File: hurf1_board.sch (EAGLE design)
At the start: 41 parts, among them IC1 STM32F10XCXT6, J1 0R, J2 0R, X1 MINI-USB-32005-201, Y1 8MHz

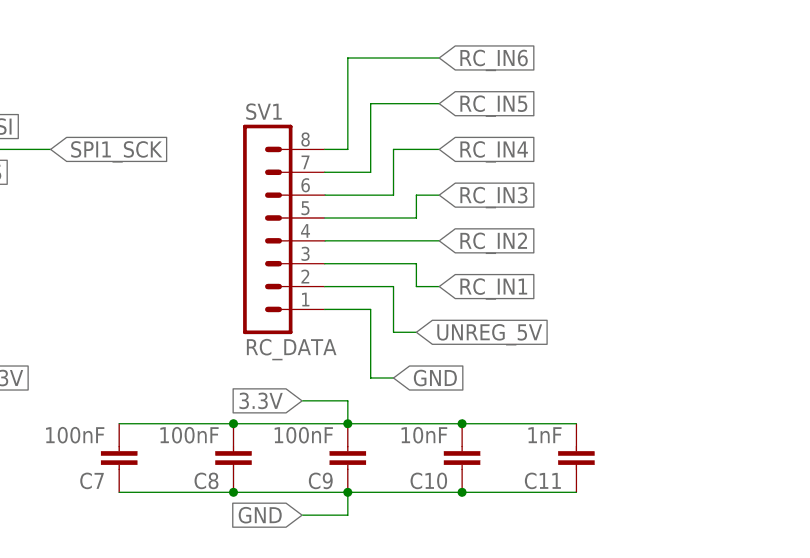
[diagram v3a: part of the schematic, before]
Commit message: Final touches to board -schematic w1 (updated)  *RC_IN port package updated from DIL -> JST-SH -board w1s1(updated)  *Schematics changes applied  *General check successful  *Signs and Logos added -Status: RTF
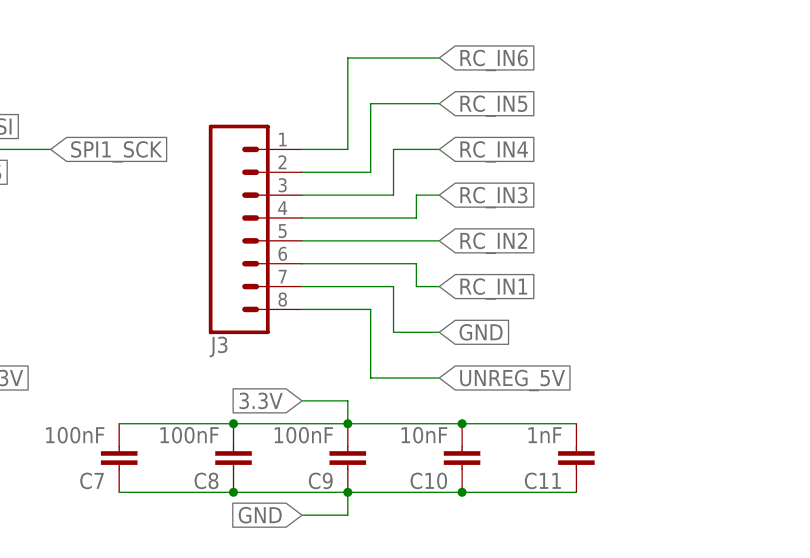
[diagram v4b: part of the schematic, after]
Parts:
- removed SV1: RC_DATA, con-lstb:MA08-1
- added J3: (no value), SparkFun-Connectors:CONN_08
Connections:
- net GND: now also J3.7; no longer SV1.1
- net RC_IN1: now also J3.6; no longer SV1.3
- net RC_IN2: now also J3.5; no longer SV1.4
- net RC_IN3: now also J3.4; no longer SV1.5
- net RC_IN4: now also J3.3; no longer SV1.6
- net RC_IN5: now also J3.2; no longer SV1.7
- net RC_IN6: now also J3.1; no longer SV1.8
- net UNREG_5V: now also J3.8; no longer SV1.2
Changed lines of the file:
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@@
 <part name="C5" library="rcl" library_urn="urn:adsk.eagle:library:334" deviceset="C-EU" device="C0603" value="100nF"/>
 <part name="C6" library="rcl" library_urn="urn:adsk.eagle:library:334" deviceset="C-EU" device="C0603" value="10nF"/>
-<part name="SV1" library="con-lstb" library_urn="urn:adsk.eagle:library:162" deviceset="MA08-1" device="" value="RC_DATA"/>
 <part name="D1" library="diode" library_urn="urn:adsk.eagle:library:210" deviceset="DIODE-2AC|CA" device="SOT23" value=" "/>
 <part name="C7" library="rcl" library_urn="urn:adsk.eagle:library:334" deviceset="C-EU" device="C0603" value="100nF"/>
@@
 <part name="ESC3" library="SparkFun-Connectors" deviceset="CONN_03" device=""/>
 <part name="ESC4" library="SparkFun-Connectors" deviceset="CONN_03" device=""/>
+<part name="J3" library="SparkFun-Connectors" deviceset="CONN_08" device=""/>
 </parts>
 <sheets>
@@
 <instance part="C5" gate="G$1" x="48.26" y="111.76"/>
 <instance part="C6" gate="G$1" x="-10.16" y="134.62"/>
-<instance part="SV1" gate="1" x="88.9" y="129.54"/>
 <instance part="D1" gate="-B1" x="53.34" y="27.94" rot="R270"/>
 <instance part="C7" gate="G$1" x="73.66" y="104.14" rot="R180"/>
@@
 <instance part="ESC3" gate="J$1" x="-53.34" y="60.96"/>
 <instance part="ESC4" gate="J$1" x="-60.96" y="48.26"/>
+<instance part="J3" gate="G$1" x="88.9" y="132.08" rot="MR180"/>
 </instances>
 <busses>
@@
 </segment>
 <segment>
-<pinref part="SV1" gate="1" pin="1"/>
-<wire x1="96.52" y1="121.92" x2="101.6" y2="121.92" width="0.1524" layer="91"/>
-<wire x1="101.6" y1="121.92" x2="101.6" y2="114.3" width="0.1524" layer="91"/>
-<wire x1="101.6" y1="114.3" x2="104.14" y2="114.3" width="0.1524" layer="91"/>
-<label x="104.14" y="114.3" size="1.778" layer="95" xref="yes"/>
+<label x="109.22" y="119.38" size="1.778" layer="95" xref="yes"/>
+<pinref part="J3" gate="G$1" pin="7"/>
+<wire x1="93.98" y1="124.46" x2="104.14" y2="124.46" width="0.1524" layer="91"/>
+<wire x1="104.14" y1="124.46" x2="104.14" y2="119.38" width="0.1524" layer="91"/>
+<wire x1="104.14" y1="119.38" x2="109.22" y2="119.38" width="0.1524" layer="91"/>
 </segment>
 <segment>
@@
 </segment>
 <segment>
-<pinref part="SV1" gate="1" pin="2"/>
-<wire x1="96.52" y1="124.46" x2="104.14" y2="124.46" width="0.1524" layer="91"/>
-<wire x1="104.14" y1="124.46" x2="104.14" y2="119.38" width="0.1524" layer="91"/>
-<wire x1="104.14" y1="119.38" x2="106.68" y2="119.38" width="0.1524" layer="91"/>
-<label x="106.68" y="119.38" size="1.778" layer="95" xref="yes"/>
+<wire x1="101.6" y1="121.92" x2="101.6" y2="114.3" width="0.1524" layer="91"/>
+<wire x1="101.6" y1="114.3" x2="109.22" y2="114.3" width="0.1524" layer="91"/>
+<label x="109.22" y="114.3" size="1.778" layer="95" xref="yes"/>
+<pinref part="J3" gate="G$1" pin="8"/>
+<wire x1="93.98" y1="121.92" x2="101.6" y2="121.92" width="0.1524" layer="91"/>
 </segment>
 <segment>
@@
 <net name="RC_IN1" class="0">
 <segment>
-<pinref part="SV1" gate="1" pin="3"/>
-<wire x1="96.52" y1="127" x2="106.68" y2="127" width="0.1524" layer="91"/>
 <wire x1="106.68" y1="127" x2="106.68" y2="124.46" width="0.1524" layer="91"/>
 <wire x1="106.68" y1="124.46" x2="109.22" y2="124.46" width="0.1524" layer="91"/>
 <label x="109.22" y="124.46" size="1.778" layer="95" xref="yes"/>
+<wire x1="93.98" y1="127" x2="106.68" y2="127" width="0.1524" layer="91"/>
+<pinref part="J3" gate="G$1" pin="6"/>
 </segment>
 <segment>
@@
 <net name="RC_IN2" class="0">
 <segment>
-<pinref part="SV1" gate="1" pin="4"/>
-<wire x1="96.52" y1="129.54" x2="109.22" y2="129.54" width="0.1524" layer="91"/>
 <label x="109.22" y="129.54" size="1.778" layer="95" xref="yes"/>
+<wire x1="109.22" y1="129.54" x2="93.98" y2="129.54" width="0.1524" layer="91"/>
+<pinref part="J3" gate="G$1" pin="5"/>
 </segment>
 <segment>
@@
 <net name="RC_IN3" class="0">
 <segment>
-<pinref part="SV1" gate="1" pin="5"/>
-<wire x1="96.52" y1="132.08" x2="106.68" y2="132.08" width="0.1524" layer="91"/>
 <wire x1="106.68" y1="132.08" x2="106.68" y2="134.62" width="0.1524" layer="91"/>
 <wire x1="106.68" y1="134.62" x2="109.22" y2="134.62" width="0.1524" layer="91"/>
 <label x="109.22" y="134.62" size="1.778" layer="95" xref="yes"/>
+<wire x1="93.98" y1="132.08" x2="106.68" y2="132.08" width="0.1524" layer="91"/>
+<pinref part="J3" gate="G$1" pin="4"/>
 </segment>
 <segment>
@@
 <net name="RC_IN4" class="0">
 <segment>
-<pinref part="SV1" gate="1" pin="6"/>
-<wire x1="96.52" y1="134.62" x2="104.14" y2="134.62" width="0.1524" layer="91"/>
 <wire x1="104.14" y1="134.62" x2="104.14" y2="139.7" width="0.1524" layer="91"/>
 <wire x1="104.14" y1="139.7" x2="109.22" y2="139.7" width="0.1524" layer="91"/>
 <label x="109.22" y="139.7" size="1.778" layer="95" xref="yes"/>
+<wire x1="93.98" y1="134.62" x2="104.14" y2="134.62" width="0.1524" layer="91"/>
+<pinref part="J3" gate="G$1" pin="3"/>
 </segment>
 <segment>
@@
 <net name="RC_IN5" class="0">
 <segment>
-<pinref part="SV1" gate="1" pin="7"/>
-<wire x1="96.52" y1="137.16" x2="101.6" y2="137.16" width="0.1524" layer="91"/>
 <wire x1="101.6" y1="137.16" x2="101.6" y2="144.78" width="0.1524" layer="91"/>
 <wire x1="101.6" y1="144.78" x2="109.22" y2="144.78" width="0.1524" layer="91"/>
 <label x="109.22" y="144.78" size="1.778" layer="95" xref="yes"/>
+<wire x1="93.98" y1="137.16" x2="101.6" y2="137.16" width="0.1524" layer="91"/>
+<pinref part="J3" gate="G$1" pin="2"/>
 </segment>
 <segment>
@@
 <net name="RC_IN6" class="0">
 <segment>
-<pinref part="SV1" gate="1" pin="8"/>
-<wire x1="96.52" y1="139.7" x2="99.06" y2="139.7" width="0.1524" layer="91"/>
 <wire x1="99.06" y1="139.7" x2="99.06" y2="149.86" width="0.1524" layer="91"/>
 <wire x1="99.06" y1="149.86" x2="109.22" y2="149.86" width="0.1524" layer="91"/>
 <label x="109.22" y="149.86" size="1.778" layer="95" xref="yes"/>
-</segment>
-<segment>
+<wire x1="93.98" y1="139.7" x2="99.06" y2="139.7" width="0.1524" layer="91"/>
+<pinref part="J3" gate="G$1" pin="1"/>
+</segment>
+<segment>

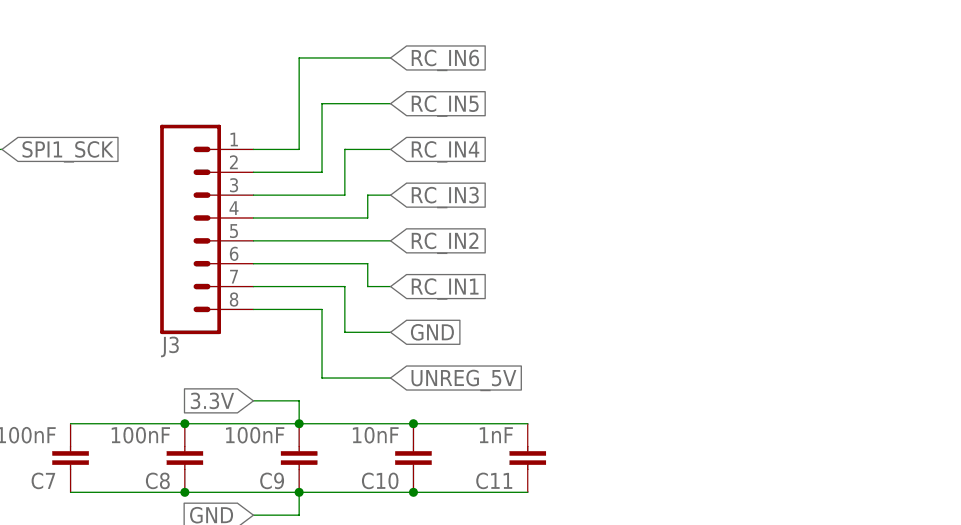
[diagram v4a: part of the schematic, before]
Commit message: Drills added , gerber out -schematic w1 (updated) -board w1s1 (updated)  *Corner Mount holes added (3mm)  *Board corners rounded  *Signs and logos rearrenged -Status : RTF =gerber_out files added
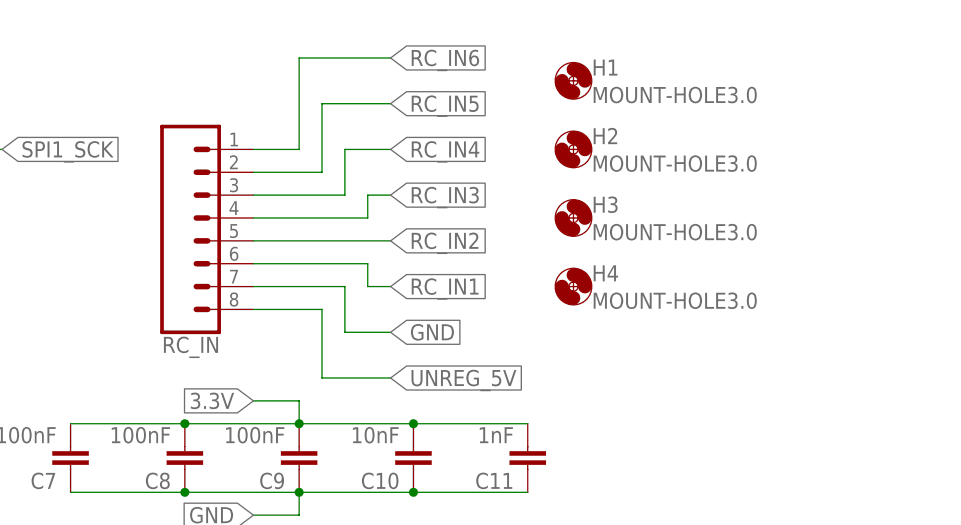
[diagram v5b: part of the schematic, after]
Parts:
- added H1, H2, H3, H4: MOUNT-HOLE3.0, holes:MOUNT-HOLE3.0
- renumbered J3 to RC_IN
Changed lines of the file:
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@@
 <part name="ESC3" library="SparkFun-Connectors" deviceset="CONN_03" device=""/>
 <part name="ESC4" library="SparkFun-Connectors" deviceset="CONN_03" device=""/>
-<part name="J3" library="SparkFun-Connectors" deviceset="CONN_08" device=""/>
+<part name="RC_IN" library="SparkFun-Connectors" deviceset="CONN_08" device=""/>
+<part name="H1" library="holes" library_urn="urn:adsk.eagle:library:237" deviceset="MOUNT-HOLE" device="3.0"/>
+<part name="H2" library="holes" library_urn="urn:adsk.eagle:library:237" deviceset="MOUNT-HOLE" device="3.0"/>
+<part name="H3" library="holes" library_urn="urn:adsk.eagle:library:237" deviceset="MOUNT-HOLE" device="3.0"/>
+<part name="H4" library="holes" library_urn="urn:adsk.eagle:library:237" deviceset="MOUNT-HOLE" device="3.0"/>
 </parts>
 <sheets>
@@
 <instance part="ESC3" gate="J$1" x="-53.34" y="60.96"/>
 <instance part="ESC4" gate="J$1" x="-60.96" y="48.26"/>
-<instance part="J3" gate="G$1" x="88.9" y="132.08" rot="MR180"/>
+<instance part="RC_IN" gate="G$1" x="88.9" y="132.08" rot="MR180"/>
+<instance part="H1" gate="G$1" x="129.54" y="147.32"/>
+<instance part="H2" gate="G$1" x="129.54" y="139.7"/>
+<instance part="H3" gate="G$1" x="129.54" y="132.08"/>
+<instance part="H4" gate="G$1" x="129.54" y="124.46"/>
 </instances>
 <busses>
@@
 <segment>
 <label x="109.22" y="119.38" size="1.778" layer="95" xref="yes"/>
-<pinref part="J3" gate="G$1" pin="7"/>
+<pinref part="RC_IN" gate="G$1" pin="7"/>
 <wire x1="93.98" y1="124.46" x2="104.14" y2="124.46" width="0.1524" layer="91"/>
 <wire x1="104.14" y1="124.46" x2="104.14" y2="119.38" width="0.1524" layer="91"/>
@@
 <wire x1="101.6" y1="114.3" x2="109.22" y2="114.3" width="0.1524" layer="91"/>
 <label x="109.22" y="114.3" size="1.778" layer="95" xref="yes"/>
-<pinref part="J3" gate="G$1" pin="8"/>
+<pinref part="RC_IN" gate="G$1" pin="8"/>
 <wire x1="93.98" y1="121.92" x2="101.6" y2="121.92" width="0.1524" layer="91"/>
 </segment>
@@
 <label x="109.22" y="124.46" size="1.778" layer="95" xref="yes"/>
 <wire x1="93.98" y1="127" x2="106.68" y2="127" width="0.1524" layer="91"/>
-<pinref part="J3" gate="G$1" pin="6"/>
+<pinref part="RC_IN" gate="G$1" pin="6"/>
 </segment>
 <segment>
@@
 <label x="109.22" y="129.54" size="1.778" layer="95" xref="yes"/>
 <wire x1="109.22" y1="129.54" x2="93.98" y2="129.54" width="0.1524" layer="91"/>
-<pinref part="J3" gate="G$1" pin="5"/>
+<pinref part="RC_IN" gate="G$1" pin="5"/>
 </segment>
 <segment>
@@
 <label x="109.22" y="134.62" size="1.778" layer="95" xref="yes"/>
 <wire x1="93.98" y1="132.08" x2="106.68" y2="132.08" width="0.1524" layer="91"/>
-<pinref part="J3" gate="G$1" pin="4"/>
+<pinref part="RC_IN" gate="G$1" pin="4"/>
 </segment>
 <segment>
@@
 <label x="109.22" y="139.7" size="1.778" layer="95" xref="yes"/>
 <wire x1="93.98" y1="134.62" x2="104.14" y2="134.62" width="0.1524" layer="91"/>
-<pinref part="J3" gate="G$1" pin="3"/>
+<pinref part="RC_IN" gate="G$1" pin="3"/>
 </segment>
 <segment>
@@
 <label x="109.22" y="144.78" size="1.778" layer="95" xref="yes"/>
 <wire x1="93.98" y1="137.16" x2="101.6" y2="137.16" width="0.1524" layer="91"/>
-<pinref part="J3" gate="G$1" pin="2"/>
+<pinref part="RC_IN" gate="G$1" pin="2"/>
 </segment>
 <segment>
@@
 <label x="109.22" y="149.86" size="1.778" layer="95" xref="yes"/>
 <wire x1="93.98" y1="139.7" x2="99.06" y2="139.7" width="0.1524" layer="91"/>
-<pinref part="J3" gate="G$1" pin="1"/>
-</segment>
-<segment>
+<pinref part="RC_IN" gate="G$1" pin="1"/>
+</segment>
+<segment>
